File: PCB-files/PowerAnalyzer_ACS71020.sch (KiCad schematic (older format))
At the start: 31 parts, among them J1 L_VinN_out, J2 L_VinL_out, J3 L_VinN_in, J4 H_VinL_in, J5 Conn_01x08, J6 Conn_01x06, U1 UCC12040, U2 ACS71020, U3 Teensy4.0, U4 Si8641

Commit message: PCB and Software Changes
PCB:
- Added a pads for pin-headers with 2.54mm pitch, for adding an external SD-card.
- Description for pins
- changed position of capacitors C1 to C4, in order to work correctly

Software:
- Added whole address R/W functions, to test the storage capabilities in the local EEPROM.
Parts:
- J6: footprint Connector_PinSocket_2.00mm:PinSocket_1x06_P2.00mm_Vertical -> Connector_PinSocket_2.54mm:PinSocket_1x06_P2.54mm_Vertical
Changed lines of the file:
@@
 Title "Power Analyzer with an ACS71020 and a Teensy"
 Date ""
-Rev "V2.0"
+Rev "V2.1"
 Comp ""
 Comment1 ""
@@
 F 0 "J6" H 9830 5242 50  0000 L CNN
 F 1 "Conn_01x06" H 9830 5151 50  0000 L CNN
-F 2 "Connector_PinSocket_2.00mm:PinSocket_1x06_P2.00mm_Vertical" H 9750 5250 50  0001 C CNN
+F 2 "Connector_PinSocket_2.54mm:PinSocket_1x06_P2.54mm_Vertical" H 9750 5250 50  0001 C CNN
 F 3 "~" H 9750 5250 50  0001 C CNN
 	1    9750 5250

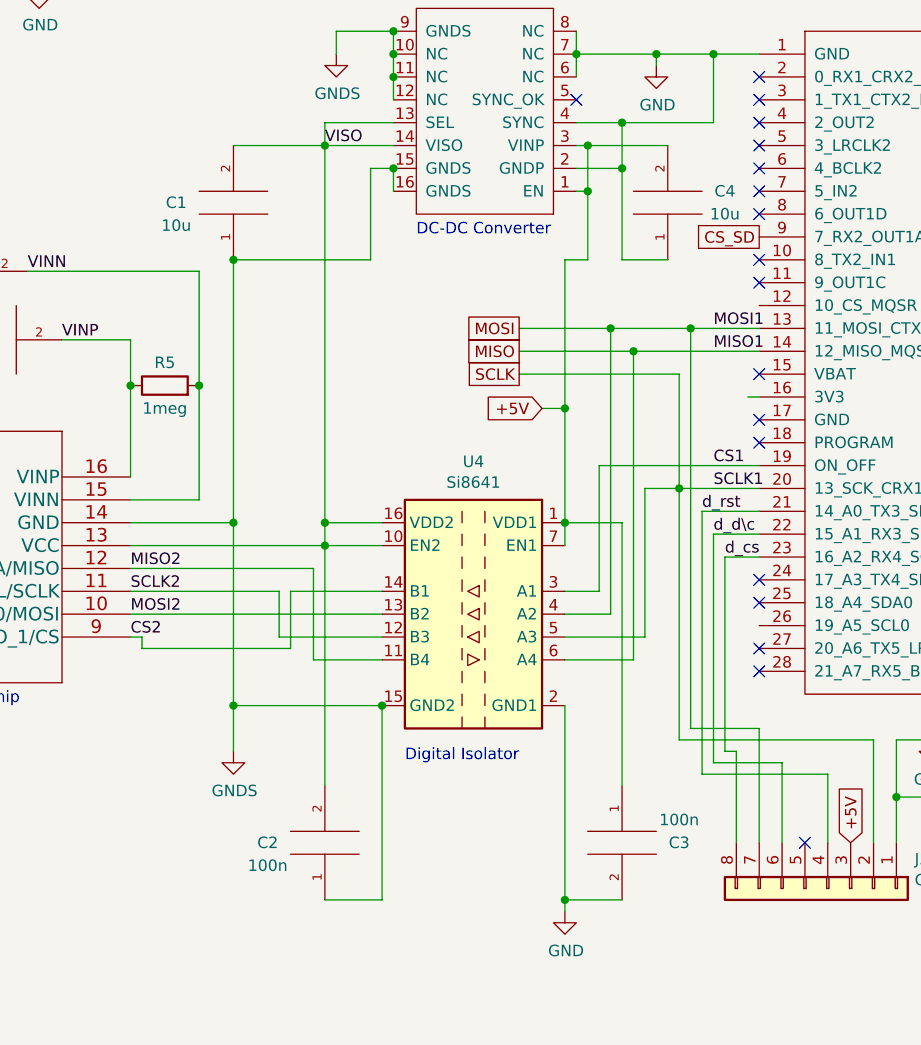
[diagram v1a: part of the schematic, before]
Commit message: PCB Updates
Mistakes in Pin-wiring corrected
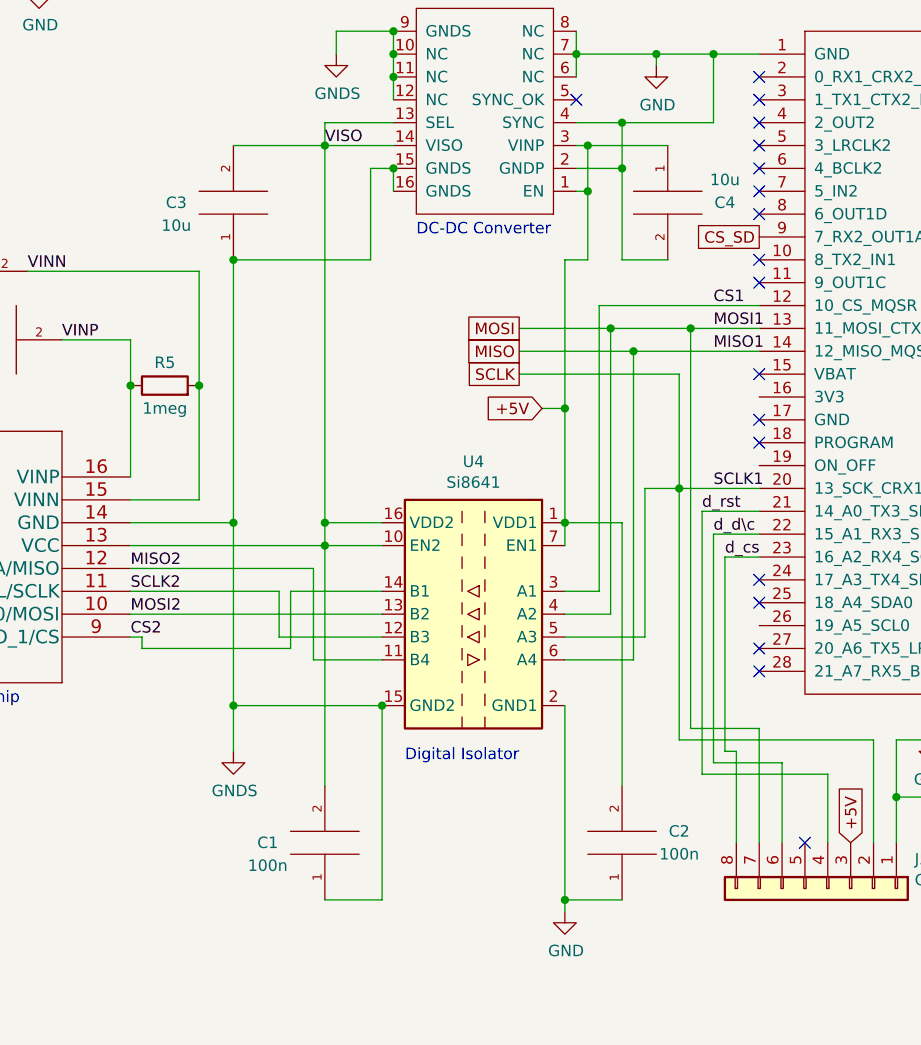
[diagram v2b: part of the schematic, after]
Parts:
- C2: renamed from C4; value 10u -> 100n
- C4: renamed from C3; value 100n -> 10u
- renumbered C2 to C1, C1 to C3
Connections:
- net CS1: now also U3.12 (10_CS_MQSR); no longer U3.19 (ON_OFF)
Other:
- moved on the sheet: C2, C4
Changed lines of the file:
@@
 Title "Power Analyzer with an ACS71020 and a Teensy"
 Date ""
-Rev "V2.1"
+Rev "V2.2"
 Comp ""
 Comment1 ""
@@
 	6400 1800 6150 1800
 $Comp
-L pspice:C C1
+L pspice:C C3
 U 1 1 5F0E6E9C
 P 5700 2550
-F 0 "C1" H 5950 2550 50  0000 C CNN
+F 0 "C3" H 5950 2550 50  0000 C CNN
 F 1 "10u" H 5950 2650 50  0000 C CNN
 F 2 "Capacitor_SMD:C_0805_2012Metric_Pad1.15x1.40mm_HandSolder" H 5700 2550 50  0001 C CNN
@@
 NoConn ~ 7200 2100
 $Comp
-L pspice:C C2
+L pspice:C C1
 U 1 1 5F1DAD16
 P 6100 5350
-F 0 "C2" H 6350 5350 50  0000 C CNN
+F 0 "C1" H 6350 5350 50  0000 C CNN
 F 1 "100n" H 6350 5450 50  0000 C CNN
 F 2 "Capacitor_SMD:C_0805_2012Metric_Pad1.15x1.40mm_HandSolder" H 6100 5350 50  0001 C CNN
@@
 Text Label 6100 2300 0    50   ~ 0
 VISO
-Text Label 7800 3700 0    50   ~ 0
+Text Label 7800 3000 0    50   ~ 0
 CS1
 Text Label 7800 3100 0    50   ~ 0
@@
 	7150 5600 7400 5600
 $Comp
-L pspice:C C3
+L pspice:C C4
 U 1 1 5F1E3B68
-P 7400 5350
-F 0 "C3" H 7650 5350 50  0000 C CNN
-F 1 "100n" H 7650 5450 50  0000 C CNN
-F 2 "Capacitor_SMD:C_0805_2012Metric_Pad1.15x1.40mm_HandSolder" H 7400 5350 50  0001 C CNN
-F 3 "~" H 7400 5350 50  0001 C CNN
-F 4 "478-12791-1-ND" H 7400 5350 50  0001 C CNN "Digikey SKU"
-	1    7400 5350
+P 7600 2550
+F 0 "C4" H 7850 2550 50  0000 C CNN
+F 1 "10u" H 7850 2650 50  0000 C CNN
+F 2 "Capacitor_SMD:C_0805_2012Metric_Pad1.15x1.40mm_HandSolder" H 7600 2550 50  0001 C CNN
+F 3 "~" H 7600 2550 50  0001 C CNN
+F 4 "478-12791-1-ND" H 7600 2550 50  0001 C CNN "Digikey SKU"
+	1    7600 2550
 	1    0    0    -1
 $EndComp
@@
 	6100 2200 6400 2200
 $Comp
-L pspice:C C4
+L pspice:C C2
 U 1 1 5F272969
-P 7600 2550
-F 0 "C4" H 7350 2500 50  0000 C CNN
-F 1 "10u" H 7350 2600 50  0000 C CNN
-F 2 "Capacitor_SMD:C_0805_2012Metric_Pad1.15x1.40mm_HandSolder" H 7600 2550 50  0001 C CNN
-F 3 "http://datasheets.avx.com/TAC.pdf" H 7600 2550 50  0001 C CNN
-F 4 " 478-2561-2-ND " H 7600 2550 50  0001 C CNN "Digikey SKU"
-	1    7600 2550
+P 7400 5350
+F 0 "C2" H 7150 5300 50  0000 C CNN
+F 1 "100n" H 7150 5400 50  0000 C CNN
+F 2 "Capacitor_SMD:C_0805_2012Metric_Pad1.15x1.40mm_HandSolder" H 7400 5350 50  0001 C CNN
+F 3 "http://datasheets.avx.com/TAC.pdf" H 7400 5350 50  0001 C CNN
+F 4 " 478-2561-2-ND " H 7400 5350 50  0001 C CNN "Digikey SKU"
+	1    7400 5350
 	-1   0    0    1
 $EndComp
@@
 	7700 4850 7700 3100
 Wire Wire Line
-	7300 3700 8000 3700
-Wire Wire Line
 	7800 4000 7800 5000
 Wire Wire Line
 	7150 4250 7300 4250
-Wire Wire Line
-	7300 3700 7300 4250
 $Comp
 L Connector:Conn_01x01_Female J2
@@
 Text GLabel 10200 4400 2    50   Output ~ 0
 3.3V
-Wire Wire Line
-	8000 3400 7950 3400
 Text GLabel 9550 5050 0    50   Input ~ 0
 3.3V
@@
 Text Notes 550  7750 0    50   ~ 0
 Copyright CERN 2013.\nThis documentation describes Open Hardware and is licensed under the CERN OHL v. 1.2.\n\nYou may redistribute and modify this documentation under the terms of the \nCERN OHL v.1.2. (http://ohwr.org/cernohl).\n\nThis documentation is distributed WITHOUT ANY EXPRESS OR IMPLIED \nWARRANTY, INCLUDING OF MERCHANTABILITY, SATISFACTORY QUALITY\nAND FITNESS FOR A PARTICULAR PURPOSE. \nPlease see the CERN OHL v.1.2 for applicable conditions
+Wire Wire Line
+	8000 3000 7300 3000
+Wire Wire Line
+	7300 3000 7300 4250
 $EndSCHEMATC
